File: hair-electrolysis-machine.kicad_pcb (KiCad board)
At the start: 2 copper layers, 53 x 53 mm, 98 parts, among them J1 USB_C_Receptacle_USB2.0_16P, J3 AudioJack2_Ground_Switch, J4 Conn_01x03_Pin, J5 Conn_01x03_Pin, J6 Conn_02x04_Odd_Even, J7 AudioJack2_Ground_Switch, Q1 BSS138, SW3 SW_SPDT, SW4 RotaryEncoder_Switch, SW5 RESET, SW6 BOOTSEL, U1 RP2040, U2 TP4054, U3 LM358B, U4 XC6206PxxxMR, U5 GD25Q64xS, U6 ADS1015IDGS, U7 MCP4725xxx-xCH, Y1 XYDBPCNANF-12MHZ

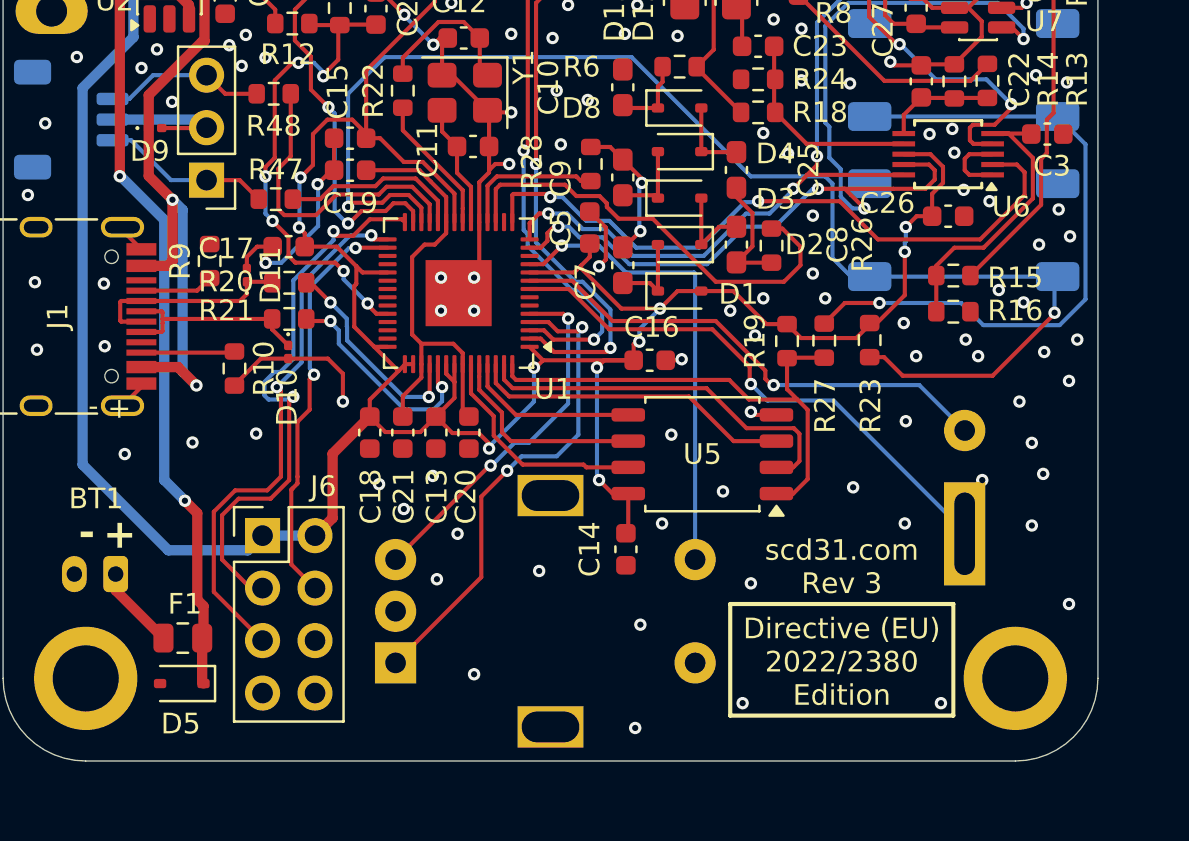
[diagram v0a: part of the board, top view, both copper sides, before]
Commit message: Changed ESD diodes and adjusted some parts
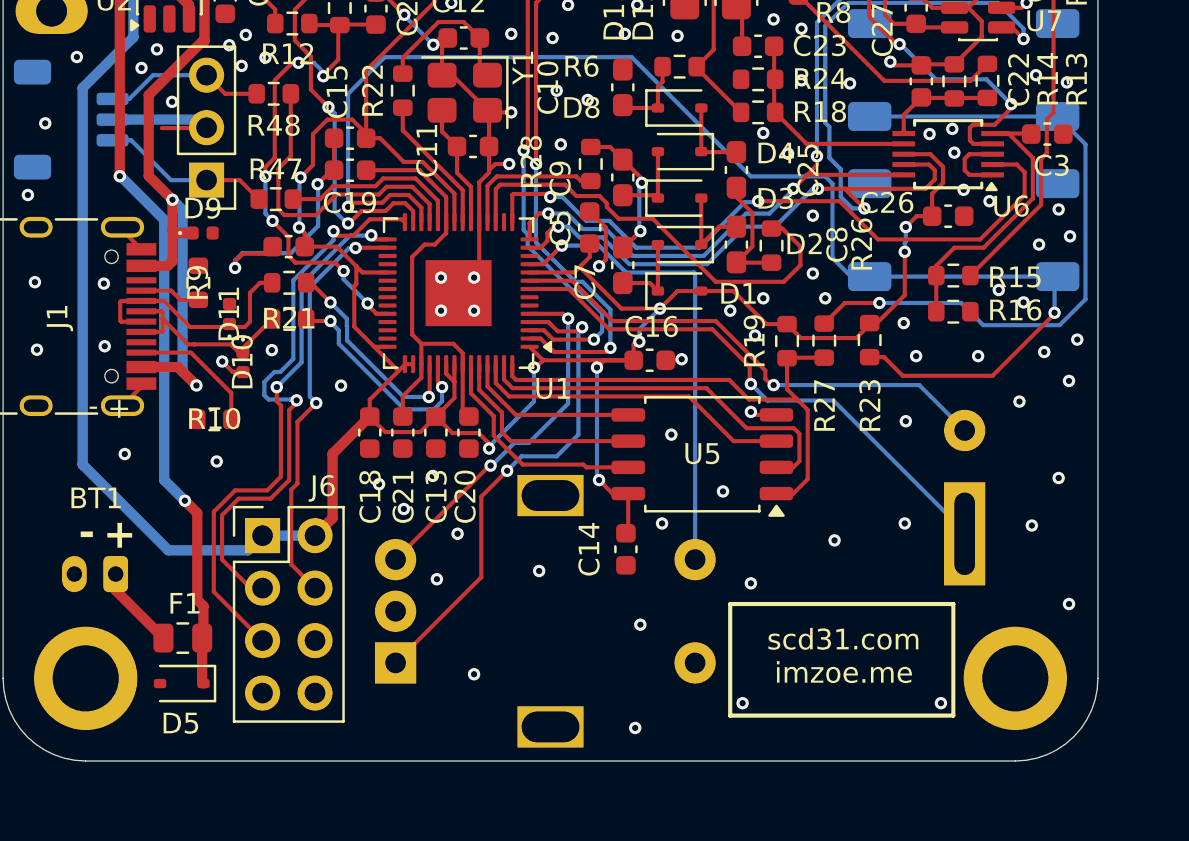
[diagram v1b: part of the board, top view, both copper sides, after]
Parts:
- C22, C23, C24, C3: value 100nF -> 0.1uF
- D10, D11, D9: footprint Diode_SMD:D_0201_0603Metric -> Diode_SMD:D_0402_1005Metric
- U5: value GD25Q64xS -> W25Q64JVSSIQ
- moved D9 5.58 mm to (132.7, 98.4)
- moved R10 2.65 mm to (133.2, 107.5), turned to 180 degrees
- moved D10 2.24 mm to (134.6, 104.7)
- moved D11 2.06 mm to (134.0, 102.4)
- moved R9 1.19 mm to (132.4, 100.8)
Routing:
- net GND: track 78.7 -> 73.7 mm, vias 142 -> 140
- net Net-(J1-CC2): track 4.53 -> 6.44 mm
- net /Mcu/D-: track 10.1 -> 11.6 mm
- net +5V: track 37.9 -> 38.9 mm
- net Net-(J1-CC1): track 3.56 -> 2.94 mm
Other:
- board text added: "scd31.com imzoe.me"
- board text removed: "Directive (EU) 2022/2380 Edition"
- board text removed: "scd31.com Rev 3"

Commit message: Updated D14 to 0402
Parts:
- D14: footprint Diode_SMD:D_0201_0603Metric -> Diode_SMD:D_0402_1005Metric
- moved D14 1.21 mm to (135.7, 81.9)
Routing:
- net /Mcu/FOOT_PEDAL: track 25.6 -> 26.7 mm
- net GND: vias 140 -> 137
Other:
- board text added: "scd31.com imzoe.me v3.4"
- board text removed: "scd31.com imzoe.me"
